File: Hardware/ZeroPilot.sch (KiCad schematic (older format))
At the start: 12 parts, among them J1 CONN_01X03, J2 CONN_01X04

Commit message: Fixed serge suggestions
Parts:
- removed D1, D2: D, Diodes_SMD:D_SOD-523, symbol D
- removed J1: CONN_01X03, Pin_Headers:Pin_Header_Straight_1x03_Pitch2.54mm, symbol CONN_01X03
- removed R1, R2: 0, Resistors_SMD:R_0603_HandSoldering, symbol R
- removed R3: 100K, Resistors_SMD:R_0603_HandSoldering, symbol R
- removed R4: 22K, Resistors_SMD:R_0603_HandSoldering, symbol R
- removed R5: 10K, Resistors_SMD:R_0603_HandSoldering, symbol R
- removed R6: 3k, Resistors_SMD:R_0603_HandSoldering, symbol R
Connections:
- wire segments 139 -> 124

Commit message: commit before my computer restarts
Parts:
- renumbered J2 to J1
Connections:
- net labels added: UHF_RX, UHF_TX
- net labels removed: REC_RX
- wire segments 124 -> 125
- no-connect marks 2 -> 1
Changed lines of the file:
@@
 encoding utf-8
 Sheet 1 21
-Title "Overall Strcture"
+Title "ZeroPilot Overview"
 Date "2017-05-14"
 Rev ""
@@
 F1 "HEADERS.sch" 60
 F2 "EXT_BATT" I R 3150 5150 60
-F3 "DBG_RX_SAFETY" I R 3150 4100 60
-F4 "DBG_TX_SAFETY" I R 3150 4000 60
+F3 "DBG_RX_SAFETY" I R 3150 3950 60
+F4 "DBG_TX_SAFETY" I R 3150 3850 60
 F5 "V_I2C" I R 3150 4400 60
 F6 "SDA1" I R 3150 6100 60
@@
 F53 "UART2_RX" I L 1350 4200 60
 F54 "UART2_CTS" I L 1350 4300 60
-F55 "DBG_RX_PILOT" I R 3150 3800 60
-F56 "DBG_TX_PILOT" I R 3150 3700 60
+F55 "DBG_RX_PILOT" I R 3150 3750 60
+F56 "DBG_TX_PILOT" I R 3150 3650 60
 F57 "NRST_PILOT" I R 3150 6950 60
 F58 "SWIO_PILOT" I R 3150 7050 60
@@
 F62 "SCLK_SAFETY" I R 3150 7500 60
 F63 "V_PROG" I R 3150 5000 60
+F64 "UHF_RX" I R 3150 4200 60
+F65 "UHF_TX" I R 3150 4100 60
 $EndSheet
 $Sheet
 S 7200 2250 1750 3950
 U 5918F046
-F0 "PILOT COTROLLER" 60
+F0 "PILOT CONTROLLER" 60
 F1 "STM32F7 IO.sch" 60
 F2 "PPM" I R 8950 2550 60
@@
 F1 "BUFFER.sch" 60
 F2 "PPM_IN" I L 7300 1450 60
-F3 "PPM_OUT" I R 8300 1450 60
-F4 "VCC" I L 7300 1900 60
-F5 "RX_IN" I L 7300 1650 60
-F6 "RX_OUT" I R 8300 1650 60
+F3 "VCC" I L 7300 1900 60
+F4 "RX_IN" I L 7300 1650 60
+F5 "PPM_OUT" O R 8300 1450 60
+F6 "RX_OUT" O R 8300 1650 60
 $EndSheet
 Text Label 7300 1900 2    60   ~ 0
@@
 Text Label 8300 1450 0    60   ~ 0
 PPM_BUFF
-Text Label 6850 1650 0    60   ~ 0
-REC_RX
 Text Label 8550 1650 2    60   ~ 0
 RX7
 Text Label 3900 1700 0    60   ~ 0
-REC_RX
+UHF_RX
 Entry Wire Line
 	6450 2700 6550 2800
@@
 Text Label 950  5550 0    59   ~ 0
 UCK2
-Text Label 3550 3450 0    59   ~ 0
+Text Label 3550 3400 0    59   ~ 0
 UART
 Entry Wire Line
-	3400 3700 3500 3600
-Entry Wire Line
-	3400 3800 3500 3700
-Text Label 3200 3700 0    59   ~ 0
+	3400 3650 3500 3550
+Entry Wire Line
+	3400 3750 3500 3650
+Text Label 3200 3650 0    59   ~ 0
 TX3
-Text Label 3200 3800 0    59   ~ 0
+Text Label 3200 3750 0    59   ~ 0
 RX3
 Text Label 4300 1300 2    59   ~ 0
 SAFETY_DBG_RX
-Text Label 3150 4100 0    59   ~ 0
+Text Label 3150 3950 0    59   ~ 0
 SAFETY_DBG_RX
 Text Label 4300 1400 2    59   ~ 0
 SAFETY_DBG_TX
-Text Label 3150 4000 0    59   ~ 0
+Text Label 3150 3850 0    59   ~ 0
 SAFETY_DBG_TX
 Text Label 650  5650 0    60   ~ 0
@@
 	1350 5550 700  5550
 Wire Bus Line
-	3500 3450 3500 3700
-Wire Bus Line
-	3500 3450 3800 3450
-Wire Wire Line
-	3400 3800 3150 3800
-Wire Wire Line
-	3150 3700 3400 3700
-Wire Wire Line
-	3150 4000 3800 4000
-Wire Wire Line
-	3150 4100 3800 4100
+	3500 3400 3500 3650
+Wire Bus Line
+	3500 3400 3800 3400
+Wire Wire Line
+	3400 3750 3150 3750
+Wire Wire Line
+	3150 3650 3400 3650
+Wire Wire Line
+	3150 3850 3800 3850
+Wire Wire Line
+	3150 3950 3800 3950
 Wire Bus Line
 	600  5650 600  7350
@@
 SCLK_SAFETY
 $Comp
-L CONN_01X04 J2
+L CONN_01X04 J1
 U 1 1 594DE28B
 P 10450 2750
-F 0 "J2" H 10450 3000 50  0000 C CNN
+F 0 "J1" H 10450 3000 50  0000 C CNN
 F 1 "CONN_01X04" V 10550 2750 50  0000 C CNN
 F 2 "Pin_Headers:Pin_Header_Straight_1x04_Pitch2.54mm" H 10450 2750 50  0001 C CNN
@@
 	1    0    0    -1
 $EndComp
-NoConn ~ 4300 1600
 NoConn ~ 4300 1800
 Text Label 5650 6950 0    60   ~ 0
@@
 3V3
 $Sheet
-S 10000 3350 750  850
+S 9900 3350 750  850
 U 59688A25
 F0 "ADC voltage dividers" 60
 F1 "ADC_voltage_dividers.sch" 60
-F2 "EXT_BATT_IN" I R 10750 3450 60
-F3 "EXT_BATT_OUT" O L 10000 3750 60
-F4 "VBATT_IN" I R 10750 3550 60
-F5 "VBATT_OUT" O L 10000 3850 60
-F6 "AIRSPD_IN" I R 10750 3650 60
-F7 "3V3" I R 10750 4100 60
-F8 "AIRSPD_OUT" O L 10000 3950 60
+F2 "EXT_BATT_IN" I R 10650 3450 60
+F3 "EXT_BATT_OUT" O L 9900 3750 60
+F4 "VBATT_IN" I R 10650 3550 60
+F5 "VBATT_OUT" O L 9900 3850 60
+F6 "AIRSPD_IN" I R 10650 3650 60
+F7 "3V3" I R 10650 4100 60
+F8 "AIRSPD_OUT" O L 9900 3950 60
 $EndSheet
 Wire Wire Line
-	10000 3950 8950 3950
-Wire Wire Line
-	8950 3850 10000 3850
-Wire Wire Line
-	10000 3750 8950 3750
-Text Label 10750 4100 0    60   ~ 0
+	9900 3950 8950 3950
+Wire Wire Line
+	8950 3850 9900 3850
+Wire Wire Line
+	9900 3750 8950 3750
+Text Label 10650 4100 0    60   ~ 0
 3V3
-Text Label 10750 3650 0    60   ~ 0
+Text Label 10650 3650 0    60   ~ 0
 AIR_SPD
-Text Label 10750 3550 0    60   ~ 0
+Text Label 10650 3550 0    60   ~ 0
 VBATT
-Text Label 10750 3450 0    60   ~ 0
+Text Label 10650 3450 0    60   ~ 0
 EXT_BATT
+Wire Wire Line
+	4300 1600 3900 1600
+Text Label 3900 1600 0    60   ~ 0
+UHF_TX
+Text Label 3150 4100 0    60   ~ 0
+UHF_TX
+Text Label 3150 4200 0    60   ~ 0
+UHF_RX
+Text Label 6850 1650 0    60   ~ 0
+UHF_RX
 $EndSCHEMATC

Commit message: routed PWM and SEL bus
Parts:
- TP1, TP2: footprint Measurement_Points:Measurement_Point_Round-SMD-Pad_Big -> Measurement_Points:Measurement_Point_Round-SMD-Pad_Small
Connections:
- no-connect marks 1 -> 0
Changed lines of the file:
@@
 F10 "REC_UART_TX" O L 4300 1600 60
 F11 "REC_UART_RX" I L 4300 1700 60
-F12 "REC_UART_CK" O L 4300 1800 60
 F13 "DBG_UART_RX" I L 4300 1300 60
 F14 "DBG_UART_TX" O L 4300 1400 60
@@
 F 0 "TP1" H 2300 1600 50  0000 C BNN
 F 1 "TEST" H 2300 1550 50  0000 C CNN
-F 2 "Measurement_Points:Measurement_Point_Round-SMD-Pad_Big" H 2300 1300 50  0001 C CNN
+F 2 "Measurement_Points:Measurement_Point_Round-SMD-Pad_Small" H 2300 1300 50  0001 C CNN
 F 3 "" H 2300 1300 50  0001 C CNN
 	1    2300 1300
@@
 F 0 "TP2" H 2450 1800 50  0000 C BNN
 F 1 "TEST" H 2450 1750 50  0000 C CNN
-F 2 "Measurement_Points:Measurement_Point_Round-SMD-Pad_Big" H 2450 1500 50  0001 C CNN
+F 2 "Measurement_Points:Measurement_Point_Round-SMD-Pad_Small" H 2450 1500 50  0001 C CNN
 F 3 "" H 2450 1500 50  0001 C CNN
 	1    2450 1500
@@
 	1    0    0    -1
 $EndComp
-NoConn ~ 4300 1800
 Text Label 5650 6950 0    60   ~ 0
 3V3

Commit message: rough power circuit routing
roughly put together the routing for power circuit, but it needs to be
replaced with thicker traces or copper pours
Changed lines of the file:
@@
 SCL1
 Text Label 3650 2000 0    60   ~ 0
-SCL1
+SCL4
 Text Label 3650 2100 0    60   ~ 0
-SDA1
+SDA4
 Entry Wire Line
 	6450 4150 6550 4250

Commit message: adc routing, made board smaller
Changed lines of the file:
@@
 F10 "REC_UART_TX" O L 4300 1600 60
 F11 "REC_UART_RX" I L 4300 1700 60
-F13 "DBG_UART_RX" I L 4300 1300 60
-F14 "DBG_UART_TX" O L 4300 1400 60
-F15 "SEL[1..12]" O R 6050 1150 60
+F12 "DBG_UART_RX" I L 4300 1300 60
+F13 "DBG_UART_TX" O L 4300 1400 60
+F14 "SEL[1..12]" O R 6050 1150 60
+F15 "MOSI" I R 6050 1400 60
+F16 "MISO" I R 6050 1500 60
+F17 "NSS" I R 6050 1600 60
+F18 "SCLK" I R 6050 1700 60
 $EndSheet
 Text Label 8950 5600 0    60   ~ 0
@@
 Text Label 6850 1650 0    60   ~ 0
 UHF_RX
+Text Label 6050 1700 0    60   ~ 0
+SCK1
+Text Label 6050 1500 0    60   ~ 0
+MISO1
+Text Label 6050 1400 0    60   ~ 0
+MOSI1
+Text Label 6050 1600 0    60   ~ 0
+NSS1
 $EndSCHEMATC

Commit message: added speaker
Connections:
- net labels added: AIRSPD_ADC, EXT_BATT_ADC, JRST, TDI, TDO, VBATT_ADC
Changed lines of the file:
@@
 Text Label 6050 1600 0    60   ~ 0
 NSS1
+Text Label 9000 3750 0    60   ~ 0
+EXT_BATT_ADC
+Text Label 9000 3850 0    60   ~ 0
+VBATT_ADC
+Text Label 9000 3950 0    60   ~ 0
+AIRSPD_ADC
+Text Label 8950 3150 0    60   ~ 0
+TDI
+Text Label 8950 3250 0    60   ~ 0
+TDO
+Text Label 8950 3450 0    60   ~ 0
+JRST
 $EndSCHEMATC

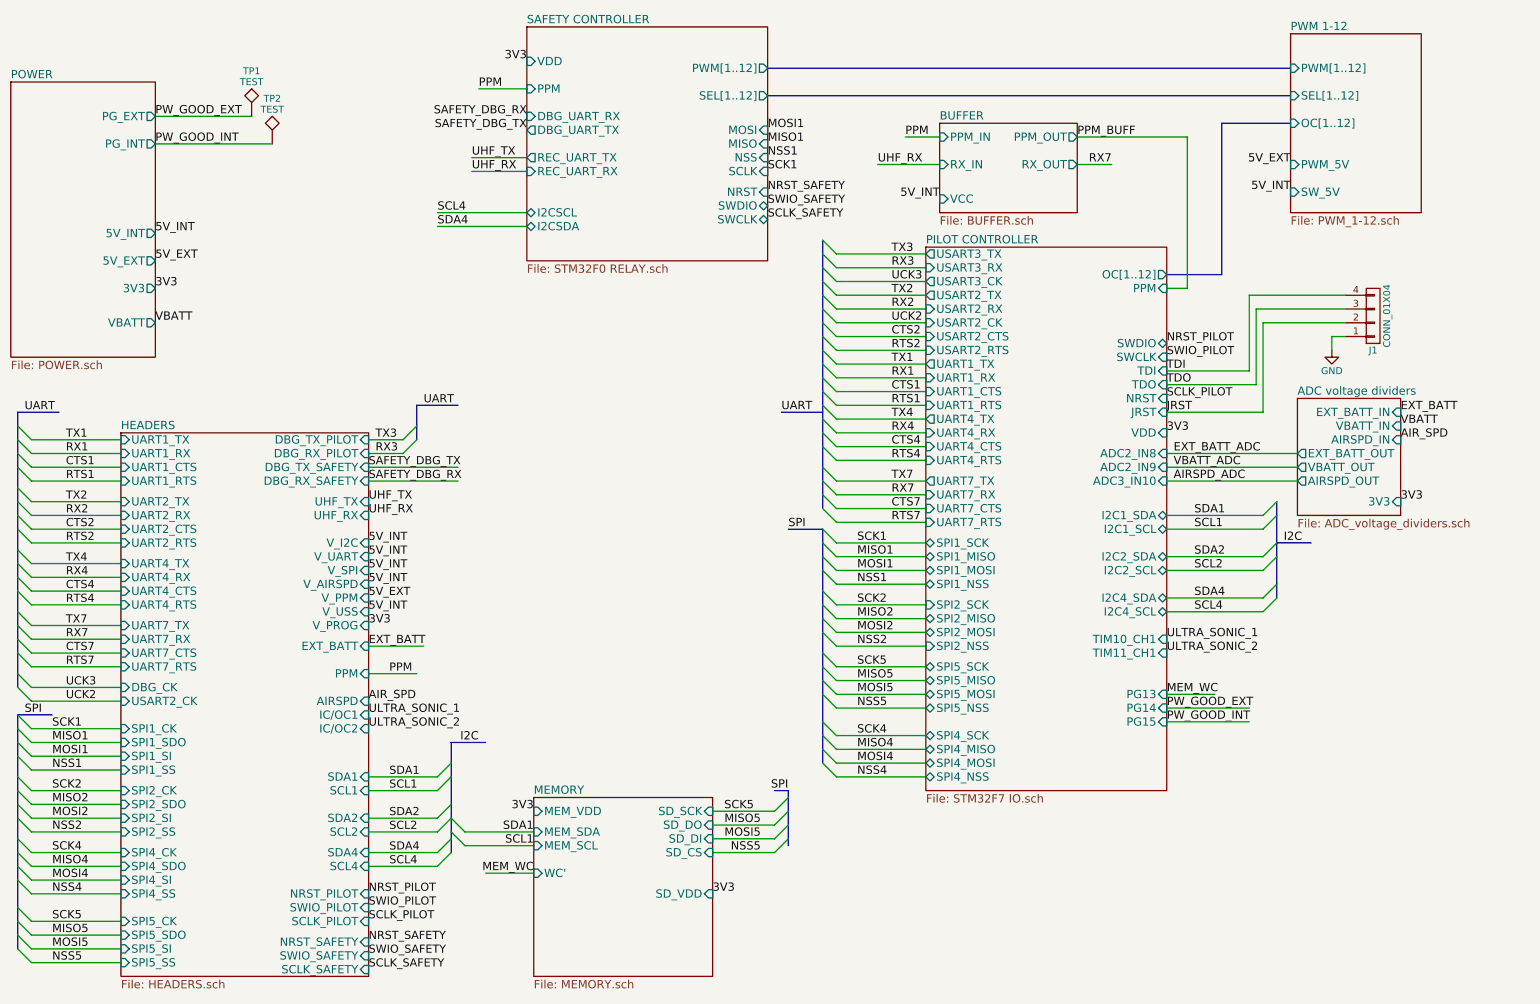
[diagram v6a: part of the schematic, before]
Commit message: Restarted work
Removed OC and SEL busses. Still need to add clocks.
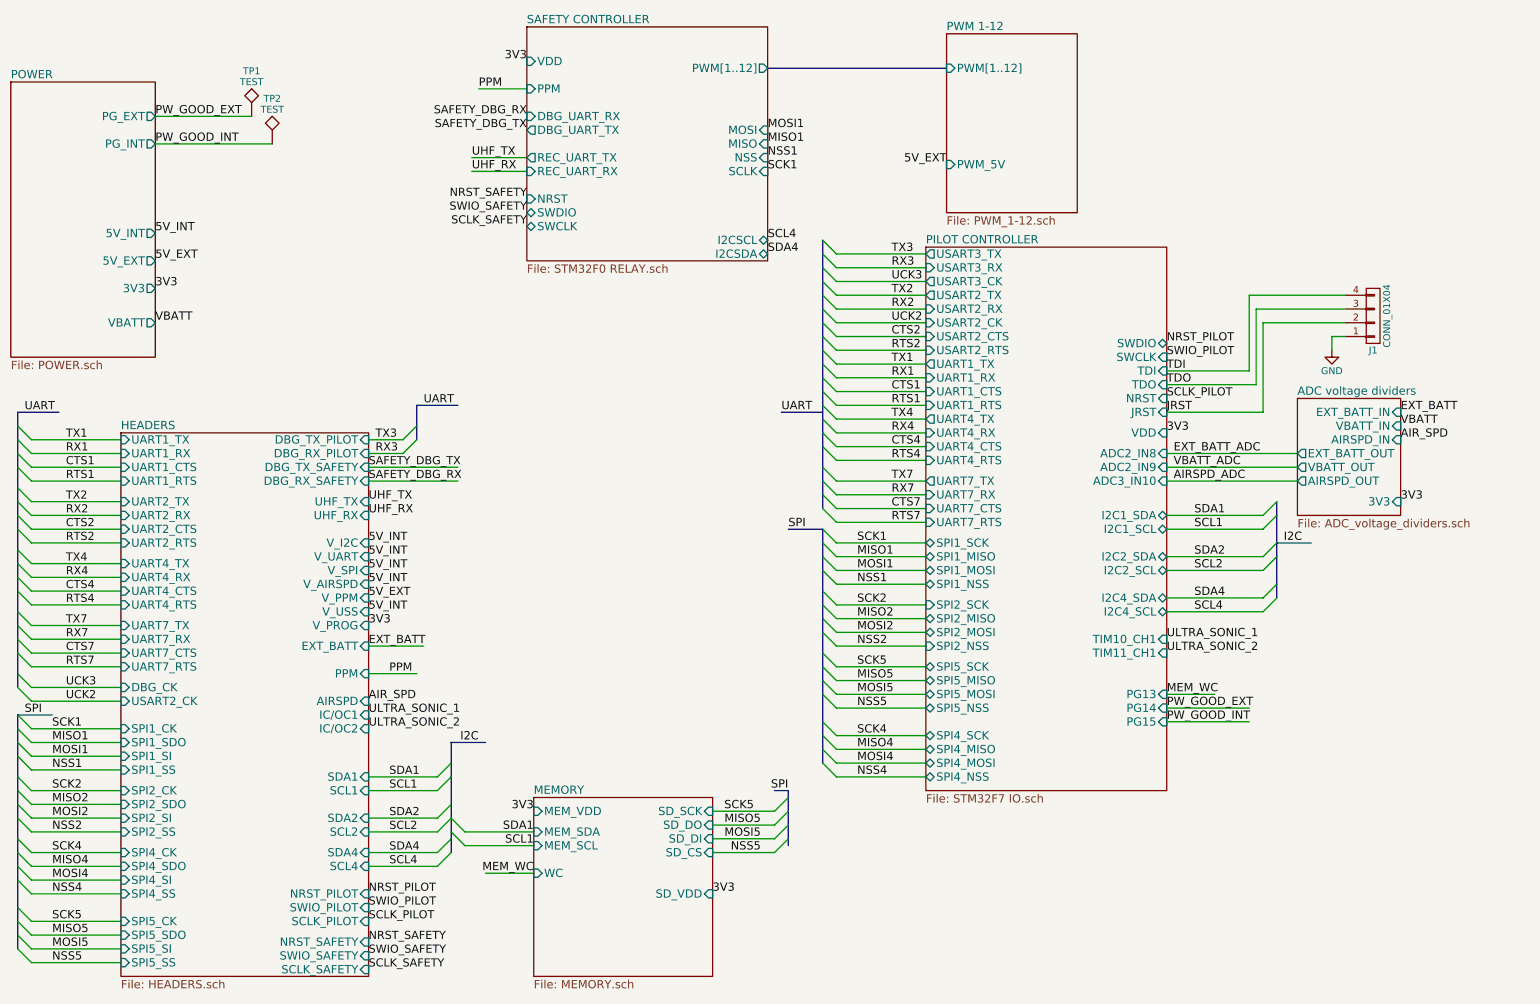
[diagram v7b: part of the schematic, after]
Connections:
- net labels removed: PPM_BUFF
- wire segments 125 -> 117

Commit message: Added clock, cleaned up files
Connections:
- wire segments 117 -> 119
